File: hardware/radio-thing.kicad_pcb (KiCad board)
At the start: 4 copper layers, 82 x 72 mm, 84 parts, among them J1 USB-C, J2 LiPo 1S, J3 ST7796 3.5in SPI, J4 RADAR HEAD, J5 DEBUG UART, Q1 AO3401A, Q2 2N7002, Q3 2N7002, SW1 PWR, SW2 RESET, SW3 BOOT, SW4 UP, SW5 DOWN, SW6 OK, SW7 BACK, SW8 MODE, U1 USBLC6-2SC6, U2 BQ24074RGT, U3 MAX17048G+T10, U4 TPS63001, U5 TPS61202, U6 ESP32-S3-WROOM-1U-N8R8, U7 ISM330DHCX, U8 LIS2MDL, U9 DWM3000

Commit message: Cut display controls to 3 buttons centred under the screen
UP / OK / DOWN on a 20 mm pitch directly below the display. Holds give the
missing actions: UP 1.5 s = cycle mode, OK 1.5 s = back, OK 3 s = sleep.
Debouncer reports hold time (new test). GPIO7/15 freed to test pads.

Co-Authored-By: Claude Opus 5.5 <noreply@anthropic.com>
Claude-Session: https://claude.ai/code/session_01Qyypna6NiNd8puVy66YruE
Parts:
- removed SW7: BACK, Button_Switch_THT:SW_PUSH-12mm
- removed SW8: MODE, Button_Switch_THT:SW_PUSH-12mm
- added TP1: IO7, TestPoint:TestPoint_Pad_D1.5mm, F.Cu at (163.9, 102.1)
- added TP2: IO15, TestPoint:TestPoint_Pad_D1.5mm, F.Cu at (167.0, 102.1)
- moved SW5 36.2 mm to (161.0, 161.0)
- moved SW4 12.5 mm to (121.0, 161.0)
- moved BZ1 3.15 mm to (164.6, 107.5)
- moved D1 3.15 mm to (165.0, 112.9)
- moved D4 3.15 mm to (164.1, 123.3)
- moved Q3 3.15 mm to (164.6, 116.4)
- moved D2 3.15 mm to (164.1, 121.1)
- moved D3 3.15 mm to (167.8, 121.1)
- moved R17 3.15 mm to (168.1, 115.1)
- moved R18 3.15 mm to (163.6, 119.2)
- moved R19 3.15 mm to (166.1, 119.2)
- moved R20 3.15 mm to (168.6, 119.2)
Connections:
- U6 pad 7: /BTN_BACK -> /SPARE_IO7
- U6 pad 8: /BTN_MODE -> /SPARE_IO15

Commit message: Hardware check: datasheet-verified fixes to charger, regulators, sensors, display, buzzer
Checked every from-memory value against manufacturer datasheets and fixed:
- BQ24074 ITERM 15k -> 3.0k (was terminating at 50%), ILIM -> ~0.9 A
- TPS63001 inductor 1.5 -> 2.2 uH, VINA RC filter; TPS61202 COUT 22 uF
- LIS2MDL C1 220 nF + 10 uF; MAX17048 VDD 100 nF
- Display (MSP3525/ST7796): powered from switched VSYS, LED pin driven
  directly (it is a logic input), SD_CS pulled high
- Buzzer from 3V3 through 15 ohm with flyback across the coil
- DWM3000 IRQ pull-down; 100 ohm series on detachable head UARTs
- M3 holes on the button tab; In2 freed for power/signal routing

Co-Authored-By: Claude Opus 5.5 <noreply@anthropic.com>
Claude-Session: https://claude.ai/code/session_01Qyypna6NiNd8puVy66YruE
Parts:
- removed Q1: AO3401A, Package_TO_SOT_SMD:SOT-23
- removed Q2: 2N7002, Package_TO_SOT_SMD:SOT-23
- removed R16: 100k, Resistor_SMD:R_0402_1005Metric
- added C25: 10u, Capacitor_SMD:C_0603_1608Metric, F.Cu at (127.3, 139.1)
- added H5: M3, MountingHole:MountingHole_3.2mm_M3, F.Cu at (103.5, 168.5)
- added H6: M3, MountingHole:MountingHole_3.2mm_M3, F.Cu at (178.5, 168.5)
- added R23: 15, Resistor_SMD:R_0402_1005Metric, F.Cu at (163.6, 112.2)
- added R24: 100, Resistor_SMD:R_0402_1005Metric, F.Cu at (124.0, 128.8)
- added R25: 100k, Resistor_SMD:R_0402_1005Metric, F.Cu at (166.6, 144.8)
- added R26: 100, Resistor_SMD:R_0402_1005Metric, F.Cu at (134.8, 101.3)
- added R27: 100, Resistor_SMD:R_0402_1005Metric, F.Cu at (137.3, 101.3)
- added R28: 100, Resistor_SMD:R_0402_1005Metric, F.Cu at (139.8, 101.3)
- added R29: 100, Resistor_SMD:R_0402_1005Metric, F.Cu at (132.3, 102.9)
- BZ1: value Magnetic 3V 6mm -> 3V magnetic transducer ~3 kHz
- C11: value 10u -> 22u
- C20: value 100n -> 220n
- C5: value 1u -> 100n
- L1: value 1.5uH 2A -> 2.2uH Isat>=2A low DCR
- R15: value 100k -> 100
- R4: value 1.5k -> 1.78k
- R6: value 15k -> 3.0k
- moved C7 14.7 mm to (110.2, 133.9)
- moved R15 6.17 mm to (169.1, 131.3)
- moved C22 2.51 mm to (169.8, 145.3)
- moved C23 2.51 mm to (173.1, 144.8)
- moved D1 2.51 mm to (167.5, 112.9)
- moved C8 2.47 mm to (113.5, 134.5)
- moved C9 2.47 mm to (117.5, 134.5)
- moved C24 1.59 mm to (134.7, 102.9)
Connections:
- BZ1 pad 1: /VSYS -> /BZ_P
- C7 pad 1: /VSYS -> /BB_VINA
- D1 pad 1: /VSYS -> /BZ_P
- J3 pad 1: /+3V3 -> /PWR_EN
- J3 pad 11: /TOUCH_CS -> unconnected-(J3-Pin_11-Pad11)
- J3 pad 14: unconnected-(J3-Pin_14-Pad14) -> /LCD_SD_CS
- J4 pad 6: /HEADA_TX -> /HA_TX_C
- J4 pad 7: /HEADA_RX -> /HA_RX_C
- J4 pad 8: /HEADB_TX -> /HB_TX_C
- J4 pad 9: /HEADB_RX -> /HB_RX_C
- R14 pad 1: /TOUCH_CS -> /LCD_SD_CS
- R15 pad 1: /BL_G -> /LCD_BL_CTL
- R15 pad 2: /+3V3 -> /LCD_LED
- U4 pad 8: /VSYS -> /BB_VINA
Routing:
- removed copper zone on In2.Cu, net /GND

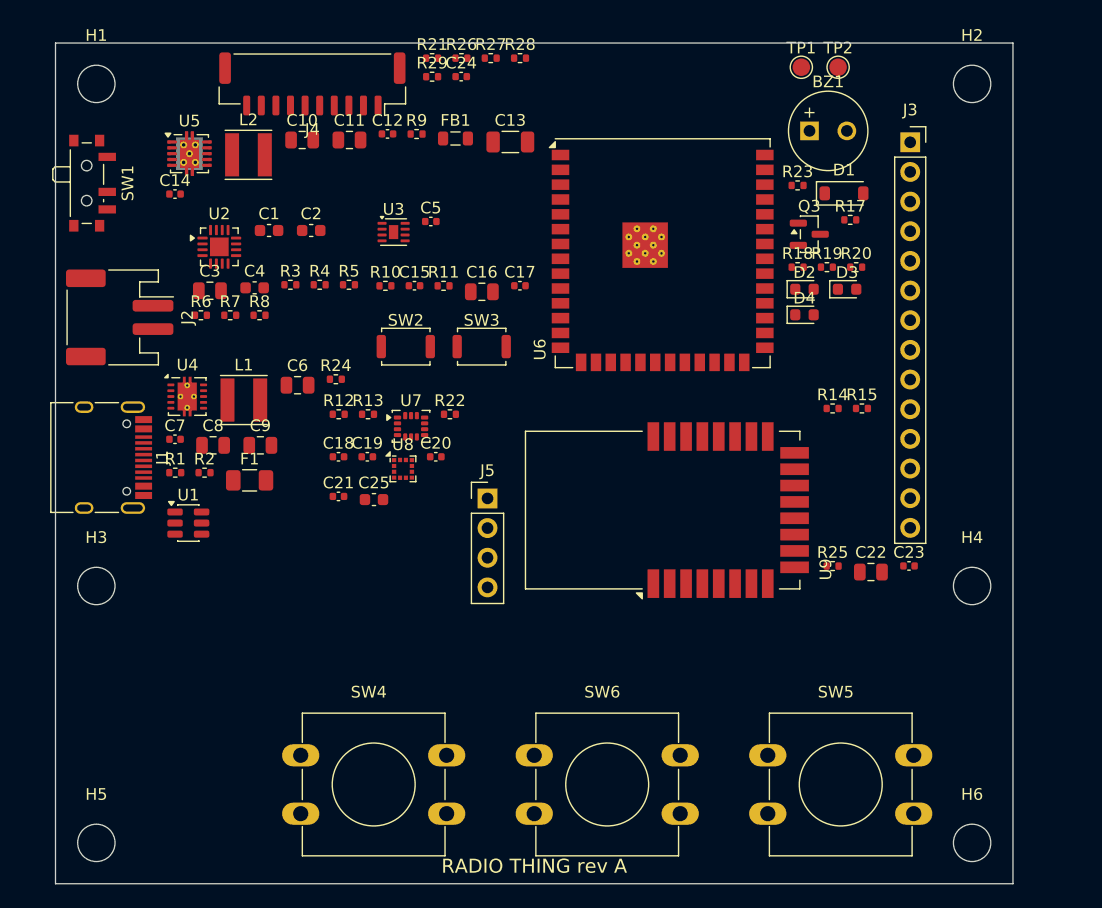
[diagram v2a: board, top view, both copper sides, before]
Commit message: Route rev A board and add manufacturing outputs
- Cluster placement: each converter's inductor and caps, the sensors'
  decoupling, USB-C parts, head-ID network and LEDs sit at their IC pins
- Two-pass Freerouting (route.sh) + GND pours: 938 segments, 108 vias,
  0 unconnected, 0 electrical DRC errors, 0 schematic-parity issues
- Button tab: routed slots + bridges instead of a V-score (a V-cut would
  sever the button traces)
- Fixed USB-C orientation-join pattern, 0.35 mm edge keep-outs, solid GND
  on IC thermal pads, 0.3 mm power traces, silkscreen tidy-up
- Optional DWM3000 footprint moved to rev B (antenna keep-out blocked routing)
- fab/: Gerber+drill zip, BOM and CPL per build variant, board-corner origin

Co-Authored-By: Claude Opus 5.5 <noreply@anthropic.com>
Claude-Session: https://claude.ai/code/session_01Qyypna6NiNd8puVy66YruE
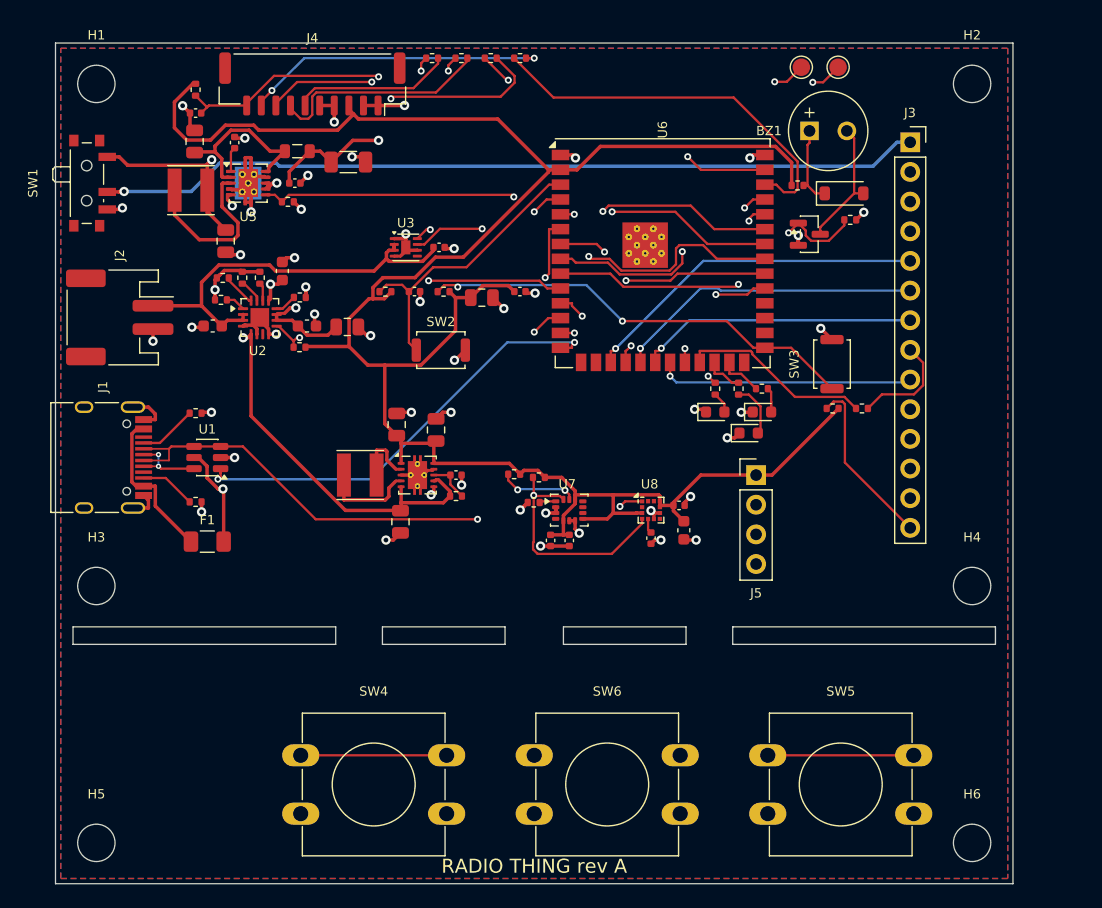
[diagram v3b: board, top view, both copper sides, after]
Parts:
- removed C22: 10u, Capacitor_SMD:C_0805_2012Metric
- removed C23: 100n, Capacitor_SMD:C_0402_1005Metric
- removed R25: 100k, Resistor_SMD:R_0402_1005Metric
- removed U9: DWM3000, RF_Module:DWM1000
- moved SW3 30.0 mm to (166.5, 127.5), turned to 90 degrees
- moved C21 29.2 mm to (153.4, 139.6)
- moved C25 26.7 mm to (153.8, 141.7), turned to -90 degrees
- moved C7 24.3 mm to (134.3, 137.0)
- moved J5 23.1 mm to (160.0, 137.0)
- moved C24 23.0 mm to (112.0, 106.0), turned to 180 degrees
- moved U8 21.5 mm to (151.0, 140.0)
- moved C18 21.0 mm to (144.0, 142.6), turned to -90 degrees
- moved U4 20.8 mm to (131.0, 137.0)
- moved R21 20.4 mm to (112.0, 104.0), turned to 90 degrees
- moved C20 19.7 mm to (151.0, 142.4), turned to -90 degrees
- moved R12 18.0 mm to (141.4, 137.2)
- moved C19 17.3 mm to (142.4, 142.6), turned to -90 degrees
- moved C8 15.8 mm to (129.2, 132.7), turned to 90 degrees
- moved U7 15.3 mm to (144.0, 140.0)
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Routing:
- net /+3V3: track 0.00 -> 185.3 mm
- net /PWR_EN: track 0.00 -> 109.5 mm, vias 0 -> 2
- net /GND: track 0.00 -> 88.6 mm, vias 0 -> 46
- net /VSYS: track 0.00 -> 85.6 mm, vias 0 -> 5
- net /BTN_DOWN: track 0.00 -> 67.9 mm, vias 0 -> 1
- net /BTN_UP: track 0.00 -> 66.0 mm, vias 0 -> 1
- net /BTN_OK: track 0.00 -> 59.3 mm, vias 0 -> 1
- net /HEAD_ID: track 0.00 -> 55.3 mm, vias 0 -> 2
- net /USB_DN: track 0.00 -> 55.0 mm, vias 0 -> 2
- net /I2C_SDA: track 0.00 -> 51.0 mm, vias 0 -> 3
- net /USB_DP: track 0.00 -> 50.5 mm, vias 0 -> 4
- net /I2C_SCL: track 0.00 -> 49.0 mm, vias 0 -> 5
- net /HEAD_EN: track 0.00 -> 45.0 mm, vias 0 -> 2
- net /HEADA_TX: track 0.00 -> 41.9 mm, vias 0 -> 2
- net /HEADA_RX: track 0.00 -> 40.0 mm, vias 0 -> 2
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- added copper zone on B.Cu, net /GND
- added copper zone on F.Cu, net /GND
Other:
- outline, holes or cut-outs redrawn
- board text added: "POD build: cut the bridges between the slots and sand flush"
- board text removed: "V-SCORE (POD build: snap off button tab)"

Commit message: Add display enclosure + button caps, recentre buttons, build guide
- enclosure/: parametric OpenSCAD front shell, lid and 3 button caps with
  STLs and previews (screen centred, ribbon to J3, board on lid posts,
  USB-C/power switch/SMA openings, tripod boss, strap slot)
- PCB: buttons centred on the enclosure centre line (board x 48.8 +/- 17.5),
  wider tab bridges, C5 moved to the MAX17048 VDD side, U3 pin-1 ground
  link; re-routed (932 segments, 107 vias, clean DRC); fab files refreshed
- route.sh: time-limited third clean-up pass with fallback
- BUILD-GUIDE.md: what the builder needs to do next

Co-Authored-By: Claude Opus 5.5 <noreply@anthropic.com>
Claude-Session: https://claude.ai/code/session_01Qyypna6NiNd8puVy66YruE
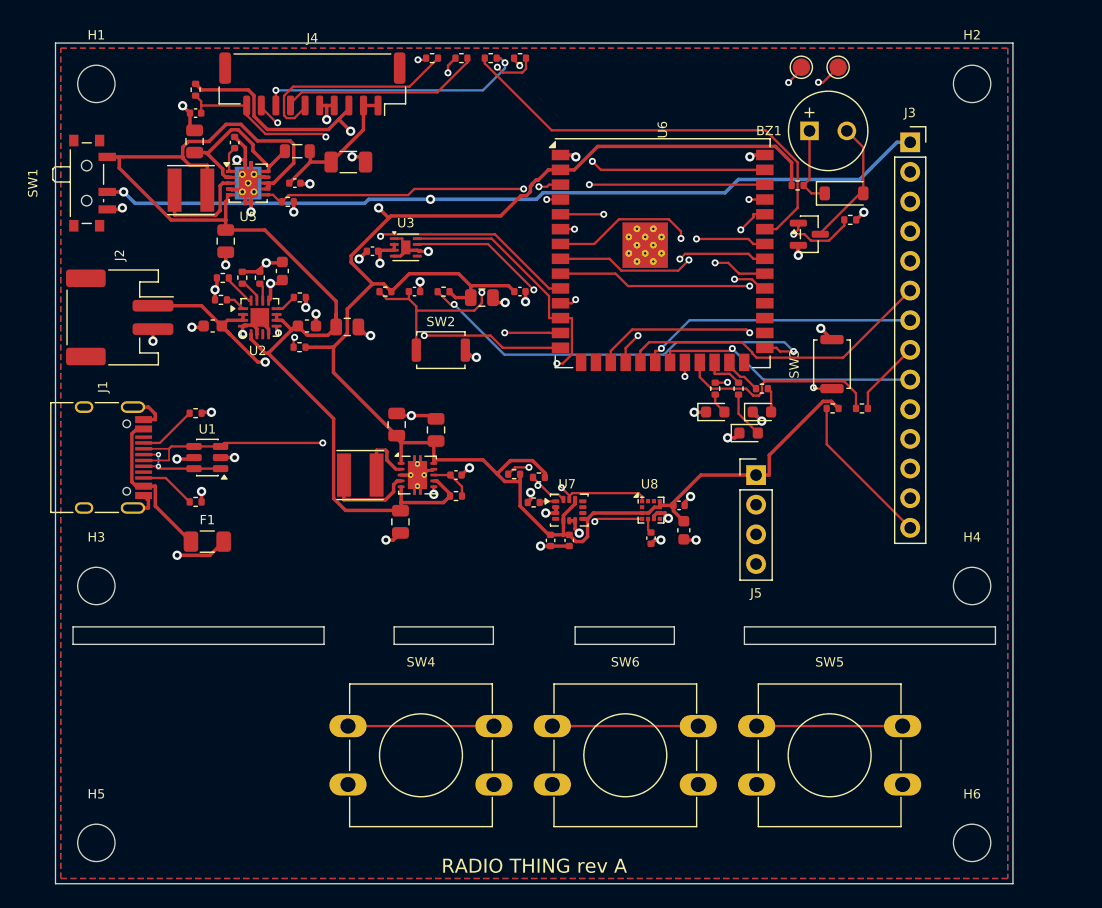
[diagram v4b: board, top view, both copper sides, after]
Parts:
- moved C5 5.71 mm to (127.2, 117.8), turned to 180 degrees
- moved SW4 4.76 mm to (125.0, 158.5)
- moved SW6 2.94 mm to (142.6, 158.5)
- moved SW5 2.67 mm to (160.1, 158.5)
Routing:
- net /VSYS: track 85.6 -> 100.5 mm, vias 5 -> 0
- net /USB_DN: track 55.0 -> 43.0 mm
- net /PWR_EN: track 109.5 -> 98.1 mm, vias 2 -> 3
- net /RST_SHARED: track 24.6 -> 34.5 mm
- net /+3V3: track 185.3 -> 175.9 mm, vias 0 -> 2
- net /HEADB_TX: track 32.3 -> 38.2 mm, vias 2 -> 0
- net /+5V_HEAD: track 17.9 -> 12.5 mm, vias 2 -> 0
- net /CHG_N: track 27.8 -> 32.9 mm, vias 2 -> 3
- net /HB_L: track 14.4 -> 9.33 mm
- net /HEADB_RX: track 33.5 -> 28.5 mm, vias 0 -> 2
- net /HA_TX_C: track 13.7 -> 18.7 mm
- net /VBUS: track 30.8 -> 35.5 mm, vias 2 -> 3
- net /BTN_UP: track 66.0 -> 61.7 mm
- net /I2C_SDA: track 51.0 -> 47.1 mm
- net /SPARE_IO7: track 27.5 -> 31.2 mm
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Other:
- outline, holes or cut-outs redrawn
